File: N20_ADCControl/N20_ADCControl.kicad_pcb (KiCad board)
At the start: 2 copper layers, 96.5 x 62 mm, 35 parts

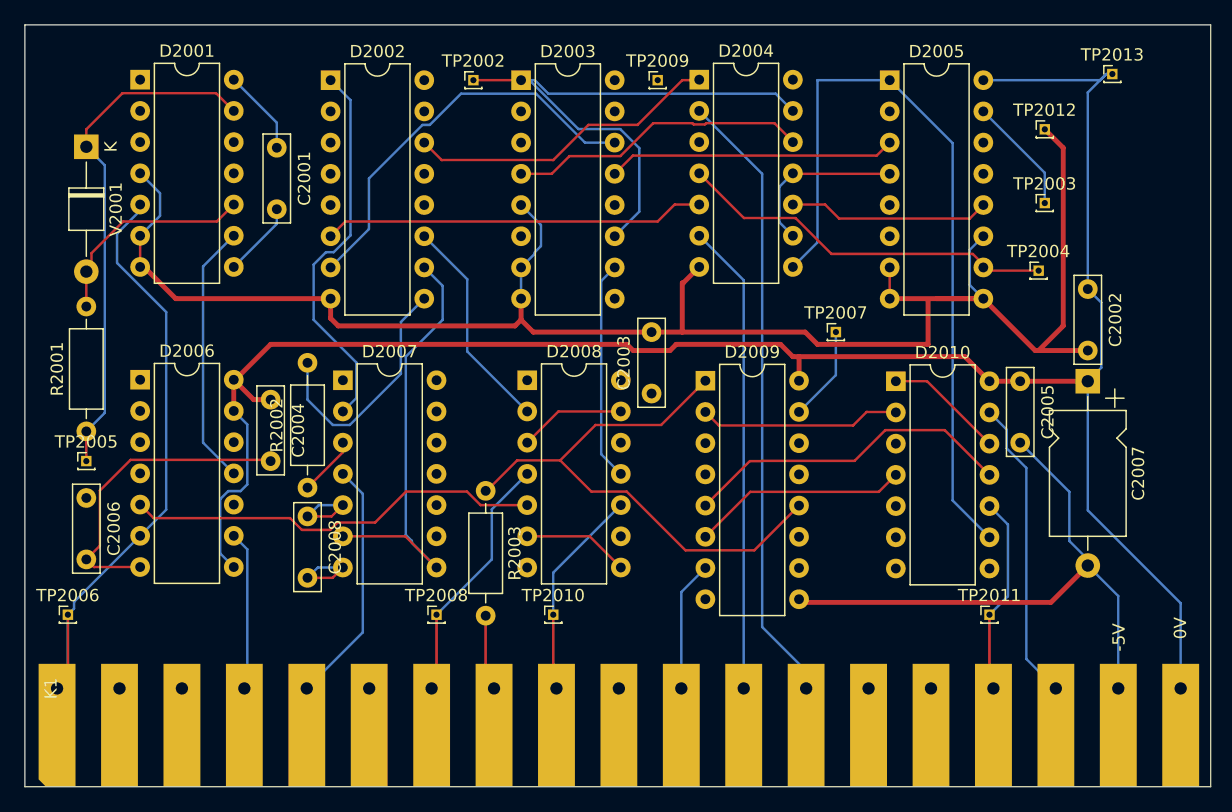
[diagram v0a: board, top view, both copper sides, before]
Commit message: Replaced testpins with testloops/beads
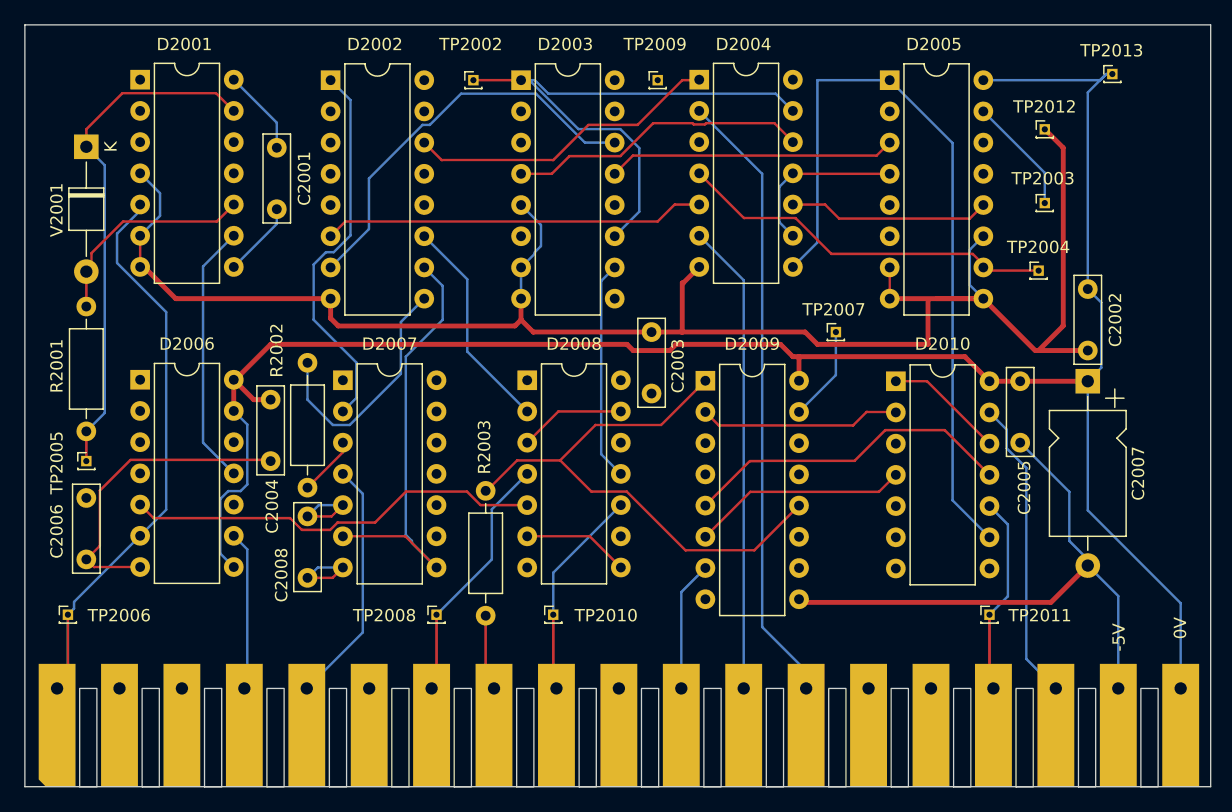
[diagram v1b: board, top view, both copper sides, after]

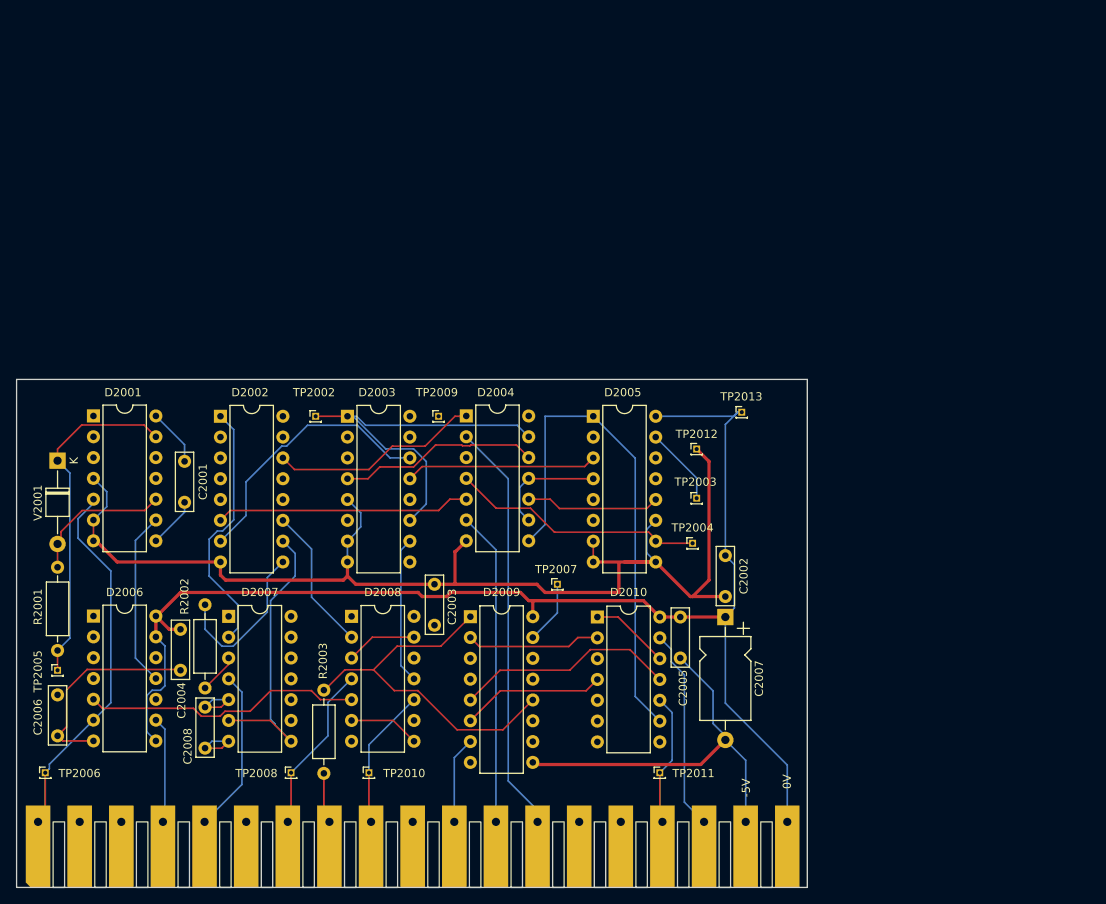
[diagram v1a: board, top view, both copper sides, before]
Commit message: Added N22/N23
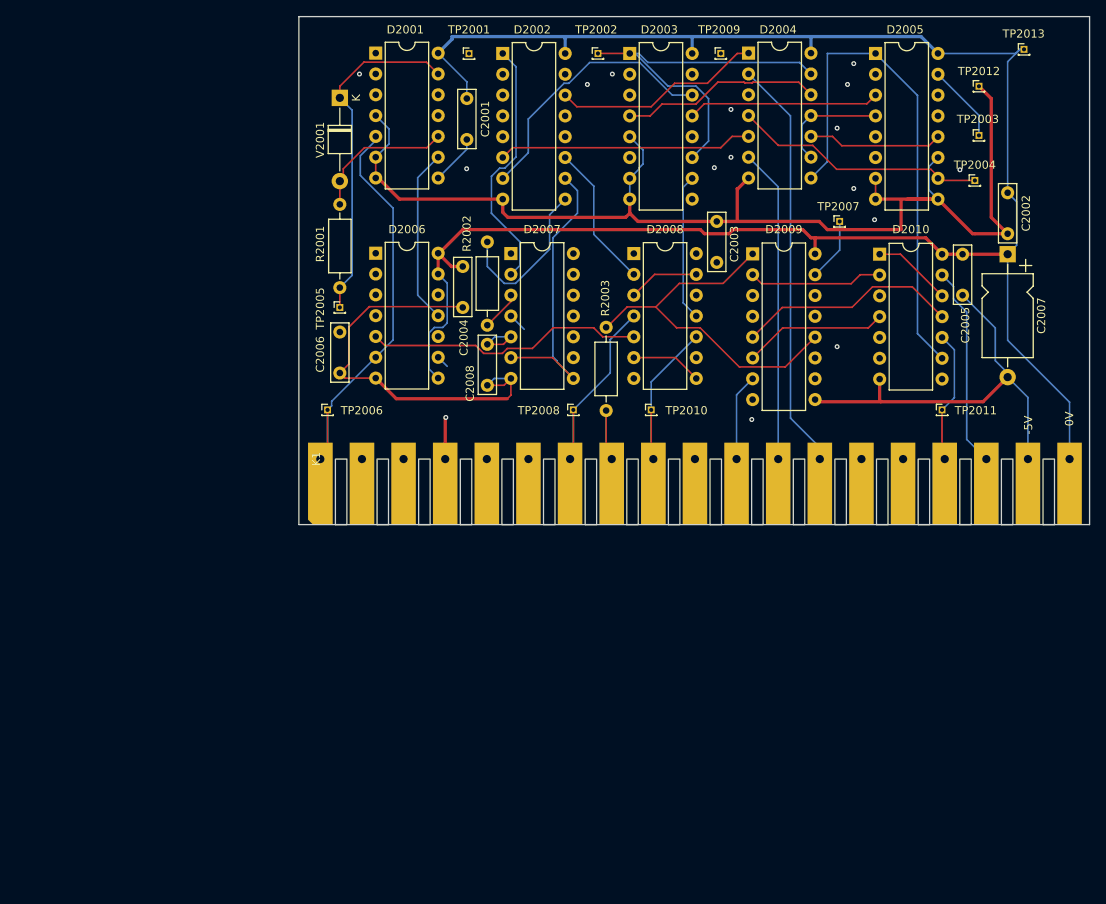
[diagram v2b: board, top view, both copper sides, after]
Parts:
- added TP2001: TestPoint, Connector_PinHeader_1.00mm:PinHeader_1x01_P1.00mm_Vertical, F.Cu at (122.7, 75.7)
- C2007: value 47u/10V -> 47u
- moved R2001 56.1 mm to (107.0, 104.3)
- moved C2001 56.1 mm to (122.5, 81.2)
- moved C2004 56.1 mm to (122.0, 101.7)
- moved C2006 56.1 mm to (107.0, 109.7)
- moved C2008 56.1 mm to (125.0, 111.2)
- moved D2002 56.1 mm to (126.8, 75.7)
- moved D2003 56.1 mm to (142.3, 75.7)
- moved D2005 56.1 mm to (172.3, 75.7)
- moved D2006 56.1 mm to (111.3, 100.1)
- moved D2009 56.1 mm to (157.3, 100.2)
- moved D2010 56.1 mm to (172.8, 100.2)
- moved R2002 56.1 mm to (125.0, 108.9)
- moved TP2005 56.1 mm to (107.0, 106.7)
- moved TP2006 56.1 mm to (105.5, 119.2)
- moved V2001 56.1 mm to (107.0, 81.1)
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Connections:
- net /C20 renamed /_C20
- net /EC20 renamed /_EC20
- net /ECP renamed /_ECP
- net /ENC20 renamed /_ENC20
- net /ERD renamed /_ERD
- net /RDY renamed /_RDY
- net /STD renamed /_STD
- net /xAZ renamed /_AZ
- net /~{RD} renamed /~{_RD}
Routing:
- net GND2: track 168.2 -> 237.3 mm
- net -5V: track 233.0 -> 255.6 mm
- net XC20: track 20.0 -> 2.29 mm
- net CP: track 13.1 -> 6.95 mm, vias 0 -> 1
- net (no net): vias 0 -> 15

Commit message: Updates, add N25
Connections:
- net AZ renamed /AZ
- net C20000 renamed /C20000
- net COMP renamed /COMP
- net CP renamed /CP
- net CPC renamed /CPC
- net DN+ renamed /DN+
- net DN- renamed /DN-
- net HSM renamed /HSM
- net POL renamed /POL
- net RC renamed /RC
- net SAZ renamed /SAZ
- net SRUP renamed /SRUP
- net UP renamed /UP
- net XC20 renamed /XC20
